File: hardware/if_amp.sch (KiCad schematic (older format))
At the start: 19 parts, among them U25 ADA4932-1

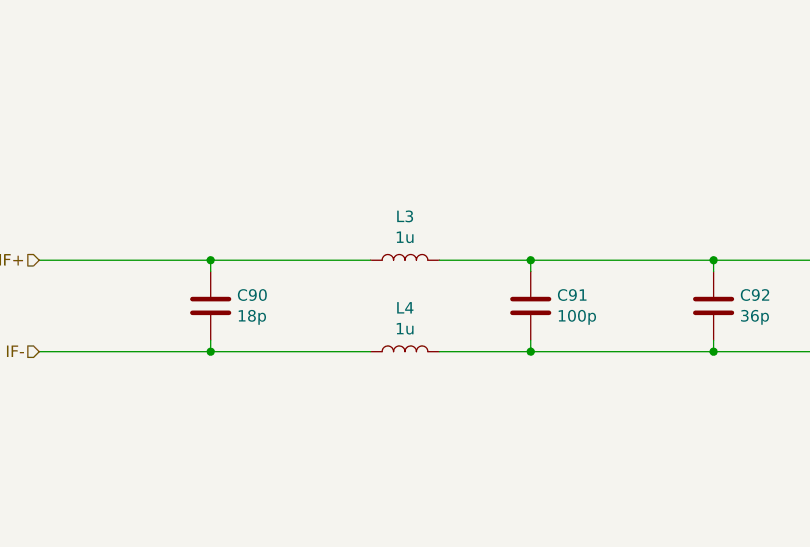
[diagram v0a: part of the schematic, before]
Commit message: updated csv file
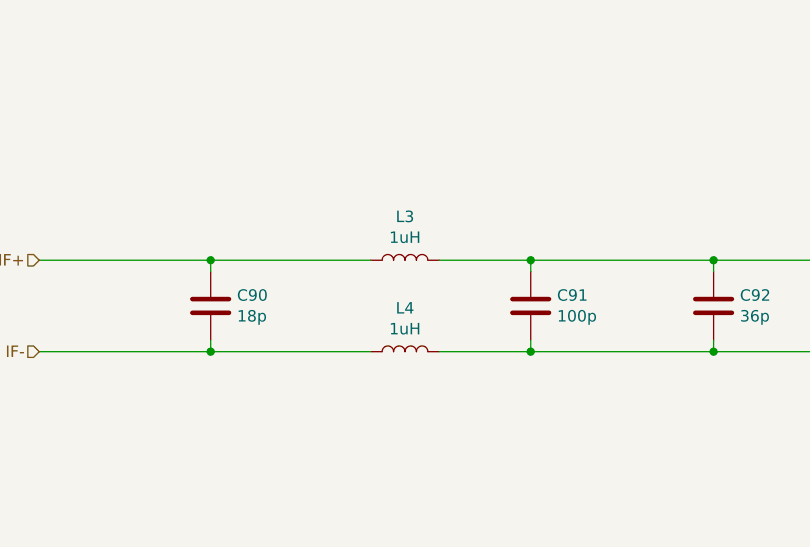
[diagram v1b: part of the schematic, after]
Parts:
- L3, L4: value 1u -> 1uH
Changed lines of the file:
@@
 P 2650 4000
 F 0 "L3" V 2840 4000 50  0000 C CNN
-F 1 "1u" V 2749 4000 50  0000 C CNN
+F 1 "1uH" V 2749 4000 50  0000 C CNN
 F 2 "violet:C_0603b" H 2650 4000 50  0001 C CNN
 F 3 "~" H 2650 4000 50  0001 C CNN
@@
 P 2650 4400
 F 0 "L4" V 2840 4400 50  0000 C CNN
-F 1 "1u" V 2749 4400 50  0000 C CNN
+F 1 "1uH" V 2749 4400 50  0000 C CNN
 F 2 "violet:C_0603b" H 2650 4400 50  0001 C CNN
 F 3 "~" H 2650 4400 50  0001 C CNN
